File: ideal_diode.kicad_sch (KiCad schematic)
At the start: 15 parts, among them Q3 NVMFS5C404NL, U7 LM74700, U8 SN74LVC2G08

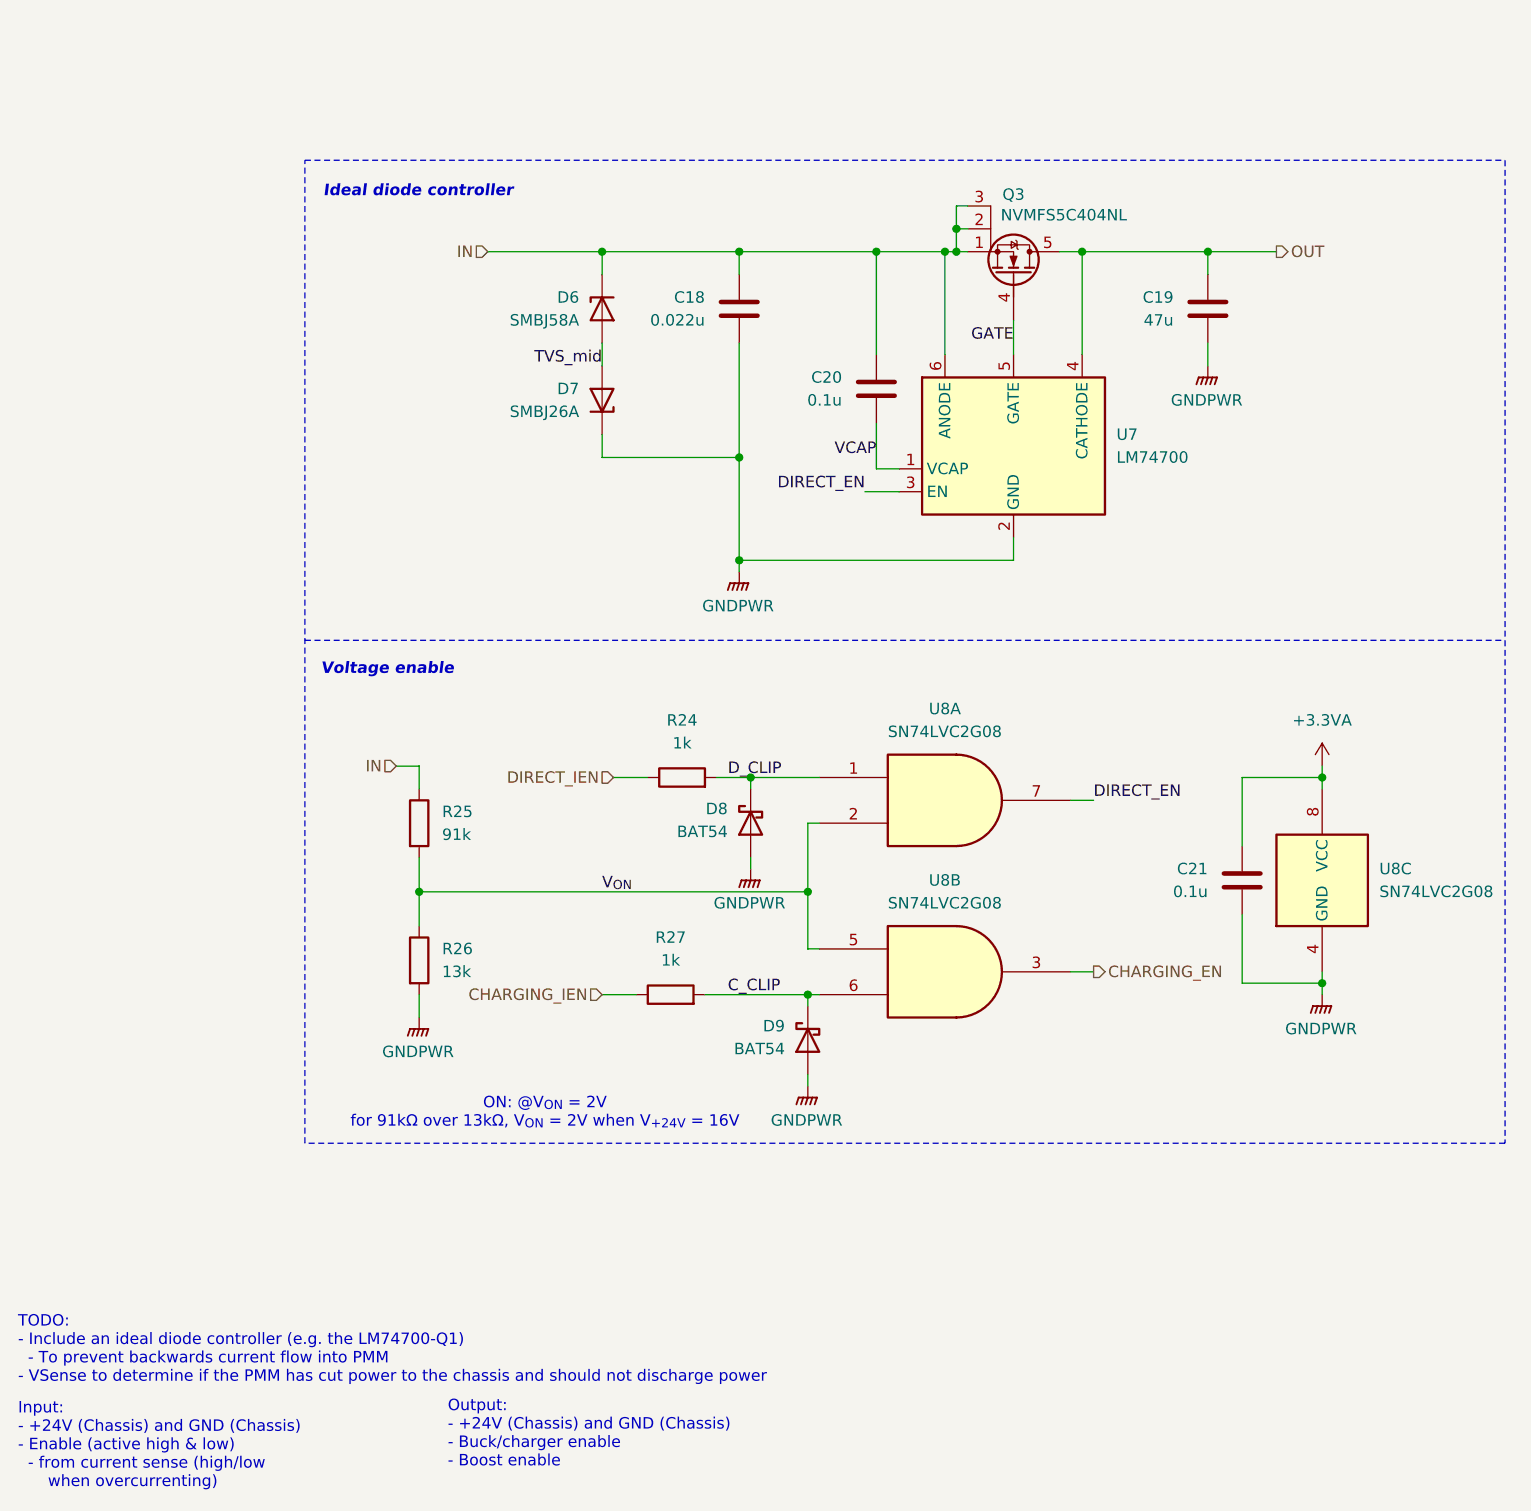
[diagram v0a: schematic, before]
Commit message: Correct symbol library path, renumber components
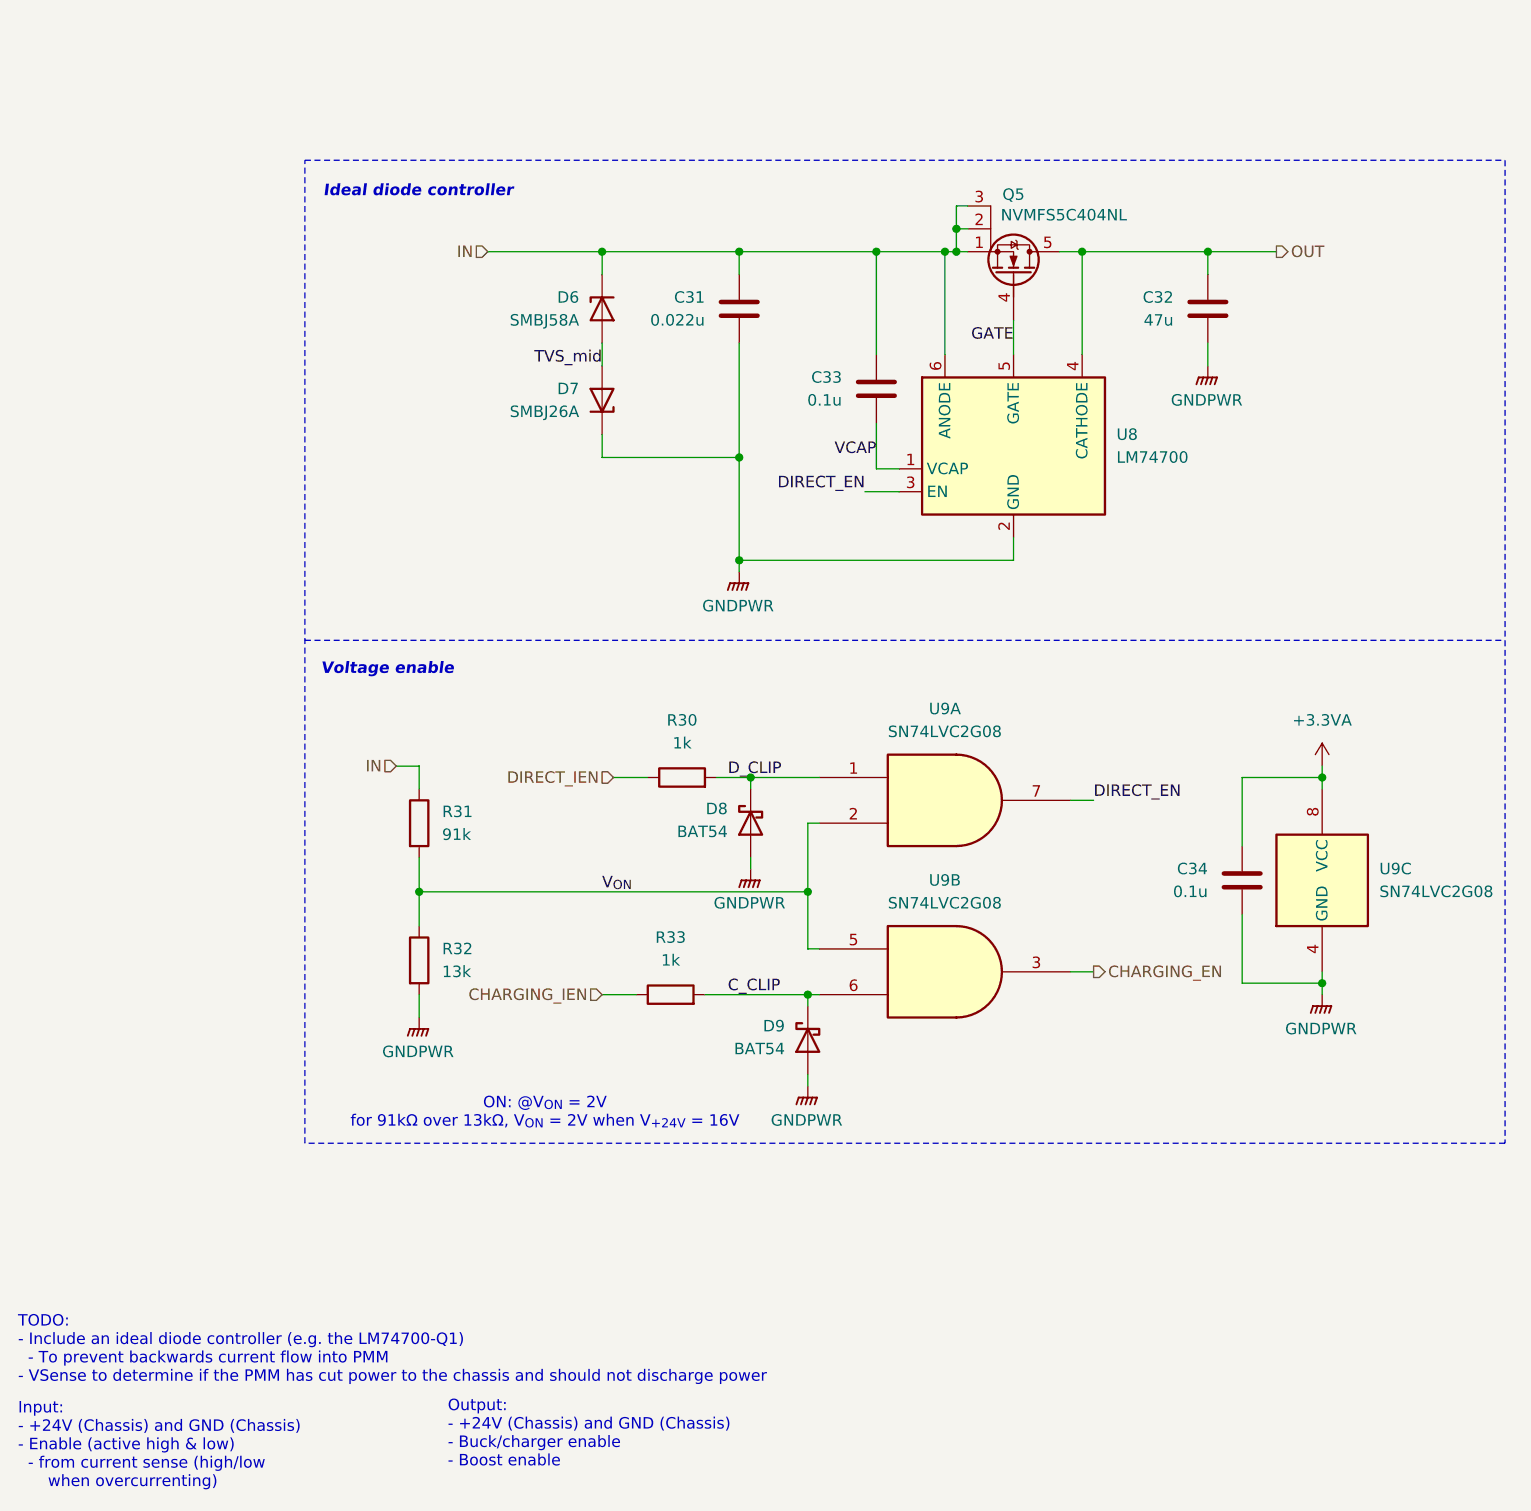
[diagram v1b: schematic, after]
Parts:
- renumbered C18 to C31, C19 to C32, C20 to C33, C21 to C34, Q3 to Q5, R24 to R30, R25 to R31, R26 to R32, R27 to R33, U7 to U8, U8 to U9
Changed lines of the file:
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@@
 		(dnp no)
 		(fields_autoplaced yes)
-		(property "Reference" "R25"
+		(property "Reference" "R31"
 			(at 91.44 110.4899 0)
 			(effects
@@
 			(project "SupercapManager"
 				(path "/6197145b-e7d4-44cc-9d90-537b6501bf60/f28a7bbd-a217-4ab0-a73c-be6ca56ea928"
-					(reference "R25")
+					(reference "R31")
 					(unit 1)
 				)
@@
 		(dnp no)
 		(fields_autoplaced yes)
-		(property "Reference" "R24"
+		(property "Reference" "R30"
 			(at 118.11 100.33 90)
 			(effects
@@
 			(project ""
 				(path "/6197145b-e7d4-44cc-9d90-537b6501bf60/f28a7bbd-a217-4ab0-a73c-be6ca56ea928"
-					(reference "R24")
+					(reference "R30")
 					(unit 1)
 				)
@@
 		(on_board yes)
 		(dnp no)
-		(property "Reference" "C19"
+		(property "Reference" "C32"
 			(at 172.72 53.3399 0)
 			(effects
@@
 			(project "SupercapManager"
 				(path "/6197145b-e7d4-44cc-9d90-537b6501bf60/f28a7bbd-a217-4ab0-a73c-be6ca56ea928"
-					(reference "C19")
+					(reference "C32")
 					(unit 1)
 				)
@@
 		(on_board yes)
 		(dnp no)
-		(property "Reference" "C18"
+		(property "Reference" "C31"
 			(at 120.65 53.3399 0)
 			(effects
@@
 			(project "SupercapManager"
 				(path "/6197145b-e7d4-44cc-9d90-537b6501bf60/f28a7bbd-a217-4ab0-a73c-be6ca56ea928"
-					(reference "C18")
+					(reference "C31")
 					(unit 1)
 				)
@@
 		(dnp no)
 		(fields_autoplaced yes)
-		(property "Reference" "R27"
+		(property "Reference" "R33"
 			(at 116.84 124.46 90)
 			(effects
@@
 			(project "SupercapManager"
 				(path "/6197145b-e7d4-44cc-9d90-537b6501bf60/f28a7bbd-a217-4ab0-a73c-be6ca56ea928"
-					(reference "R27")
+					(reference "R33")
 					(unit 1)
 				)
@@
 		(dnp no)
 		(fields_autoplaced yes)
-		(property "Reference" "U8"
+		(property "Reference" "U9"
 			(at 147.3089 118.11 0)
 			(effects
@@
 			(project ""
 				(path "/6197145b-e7d4-44cc-9d90-537b6501bf60/f28a7bbd-a217-4ab0-a73c-be6ca56ea928"
-					(reference "U8")
+					(reference "U9")
 					(unit 2)
 				)
@@
 		(on_board yes)
 		(dnp no)
-		(property "Reference" "C20"
+		(property "Reference" "C33"
 			(at 135.89 62.2299 0)
 			(effects
@@
 			(project "SupercapManager"
 				(path "/6197145b-e7d4-44cc-9d90-537b6501bf60/f28a7bbd-a217-4ab0-a73c-be6ca56ea928"
-					(reference "C20")
+					(reference "C33")
 					(unit 1)
 				)
@@
 		(on_board yes)
 		(dnp no)
-		(property "Reference" "Q3"
+		(property "Reference" "Q5"
 			(at 154.94 41.91 90)
 			(effects
@@
 			(project "SupercapManager"
 				(path "/6197145b-e7d4-44cc-9d90-537b6501bf60/f28a7bbd-a217-4ab0-a73c-be6ca56ea928"
-					(reference "Q3")
+					(reference "Q5")
 					(unit 1)
 				)
@@
 		(dnp no)
 		(fields_autoplaced yes)
-		(property "Reference" "U7"
+		(property "Reference" "U8"
 			(at 166.37 68.5799 0)
 			(effects
@@
 			(project ""
 				(path "/6197145b-e7d4-44cc-9d90-537b6501bf60/f28a7bbd-a217-4ab0-a73c-be6ca56ea928"
-					(reference "U7")
+					(reference "U8")
 					(unit 1)
 				)
@@
 		(dnp no)
 		(fields_autoplaced yes)
-		(property "Reference" "U8"
+		(property "Reference" "U9"
 			(at 195.58 116.8399 0)
 			(effects
@@
 			(project ""
 				(path "/6197145b-e7d4-44cc-9d90-537b6501bf60/f28a7bbd-a217-4ab0-a73c-be6ca56ea928"
-					(reference "U8")
+					(reference "U9")
 					(unit 3)
 				)
@@
 		(dnp no)
 		(fields_autoplaced yes)
-		(property "Reference" "R26"
+		(property "Reference" "R32"
 			(at 91.44 125.7299 0)
 			(effects
@@
 			(project "SupercapManager"
 				(path "/6197145b-e7d4-44cc-9d90-537b6501bf60/f28a7bbd-a217-4ab0-a73c-be6ca56ea928"
-					(reference "R26")
+					(reference "R32")
 					(unit 1)
 				)
@@
 		(on_board yes)
 		(dnp no)
-		(property "Reference" "C21"
+		(property "Reference" "C34"
 			(at 176.53 116.8399 0)
 			(effects
@@
 			(project "SupercapManager"
 				(path "/6197145b-e7d4-44cc-9d90-537b6501bf60/f28a7bbd-a217-4ab0-a73c-be6ca56ea928"
-					(reference "C21")
+					(reference "C34")
 					(unit 1)
 				)
@@
 		(dnp no)
 		(fields_autoplaced yes)
-		(property "Reference" "U8"
+		(property "Reference" "U9"
 			(at 147.3089 99.06 0)
 			(effects
@@
 			(project ""
 				(path "/6197145b-e7d4-44cc-9d90-537b6501bf60/f28a7bbd-a217-4ab0-a73c-be6ca56ea928"
-					(reference "U8")
-					(unit 1)
-				)
+					(reference "U9")
+					(unit 1)
+				)

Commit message: Fix broken component links
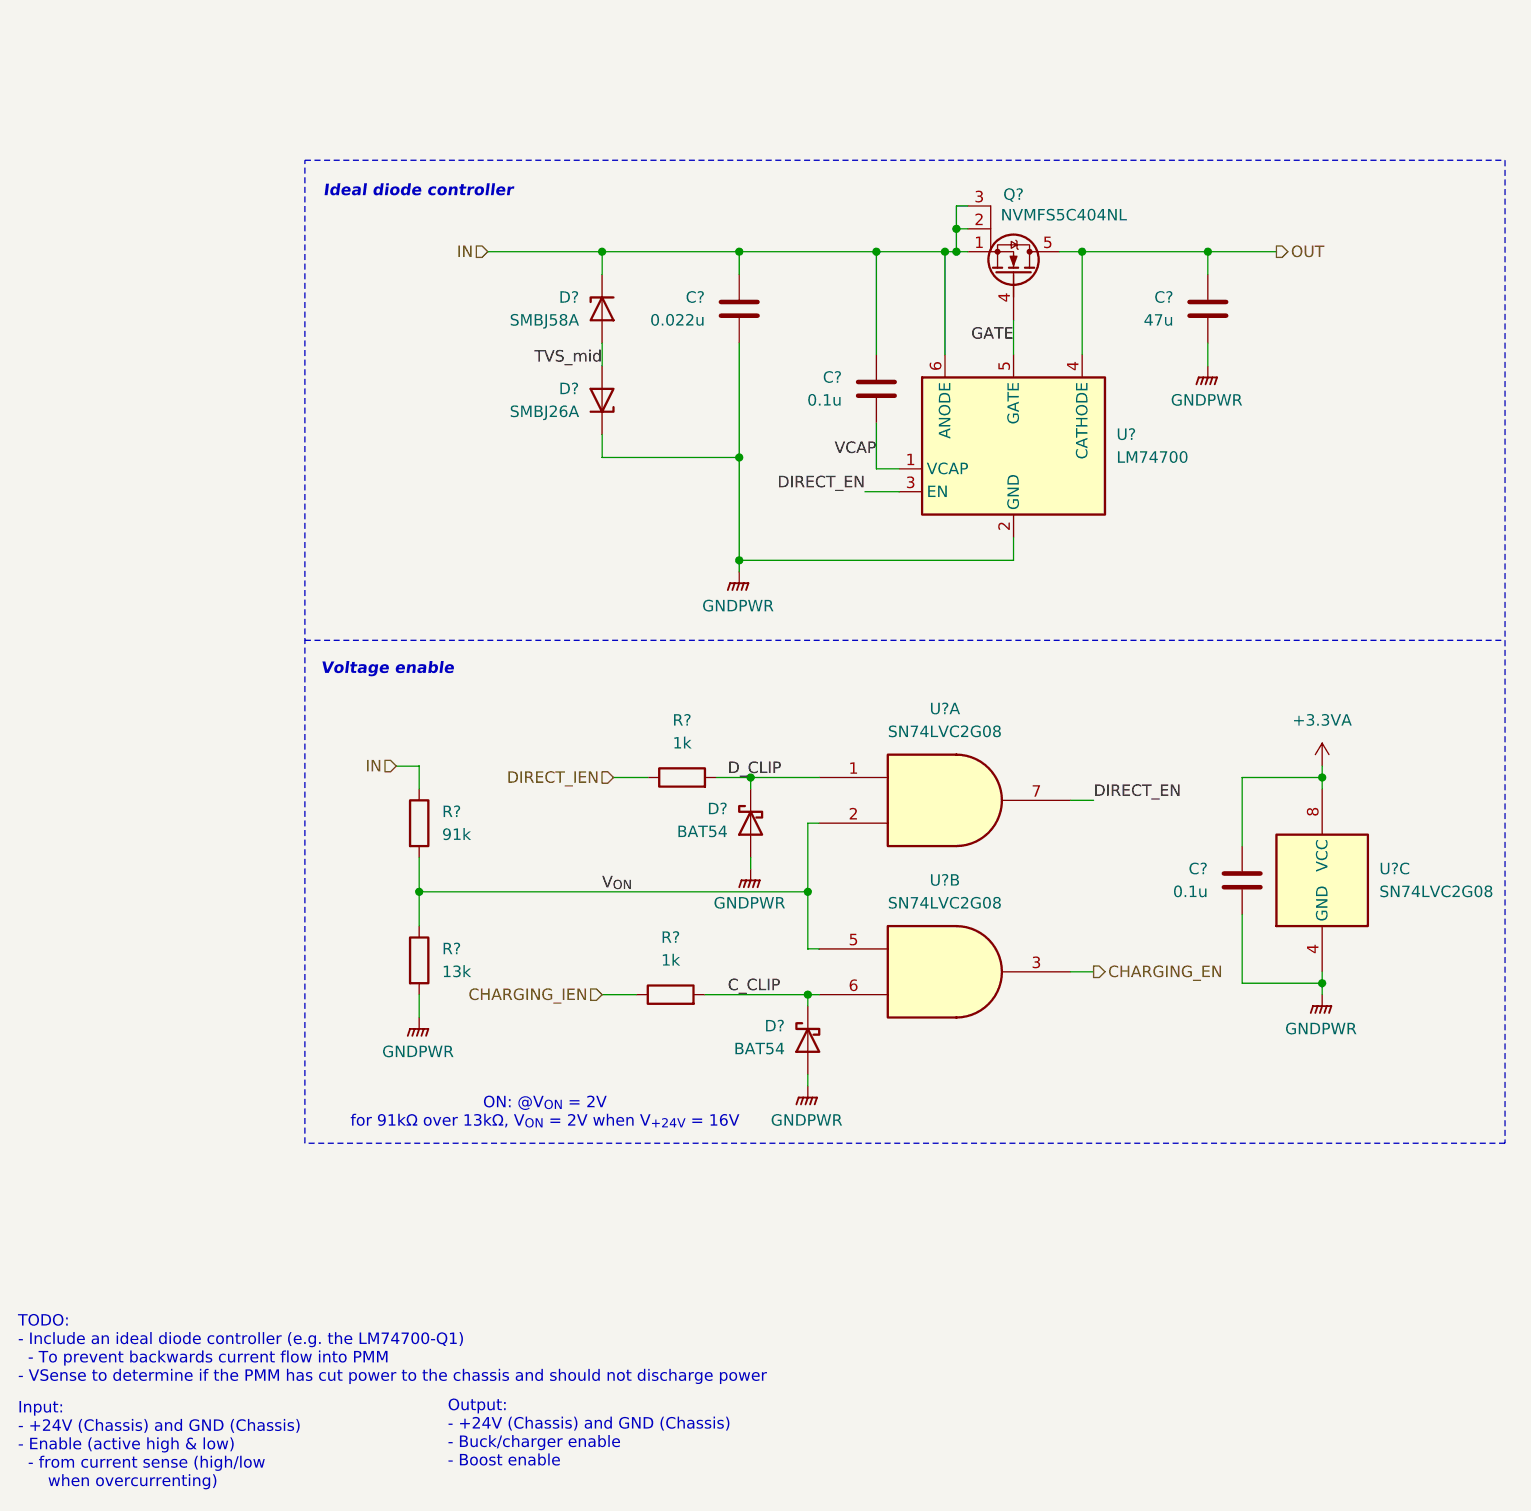
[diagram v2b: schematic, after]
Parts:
- renumbered C32 to C?, C31 to C?, C33 to C?, C34 to C?, D8 to D?, D9 to D?, D6 to D?, D7 to D?, Q5 to Q?, R31 to R?, R30 to R?, R33 to R?, R32 to R?, U9 to U?, U8 to U?
